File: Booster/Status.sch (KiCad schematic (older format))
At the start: 31 parts, among them J601 StatusLED, P601 ~OVERCURRENT_OUT, P602 ~OVERCURRENT_OUT_OP, P603 MSTR_SW, P604 MSTR_SW_OUT, P605 MSTR_SW_OUT_OP, P606 DRIVER_ENABLE_OUT_OP, P607 DRIVER_ENABLE_OUT, Q601 BC327, Q602 BC327, Q603 BC327, SW601 MSTR_SW, U601 74HC00, U602 PC817, U603 PC817, U604 PC817

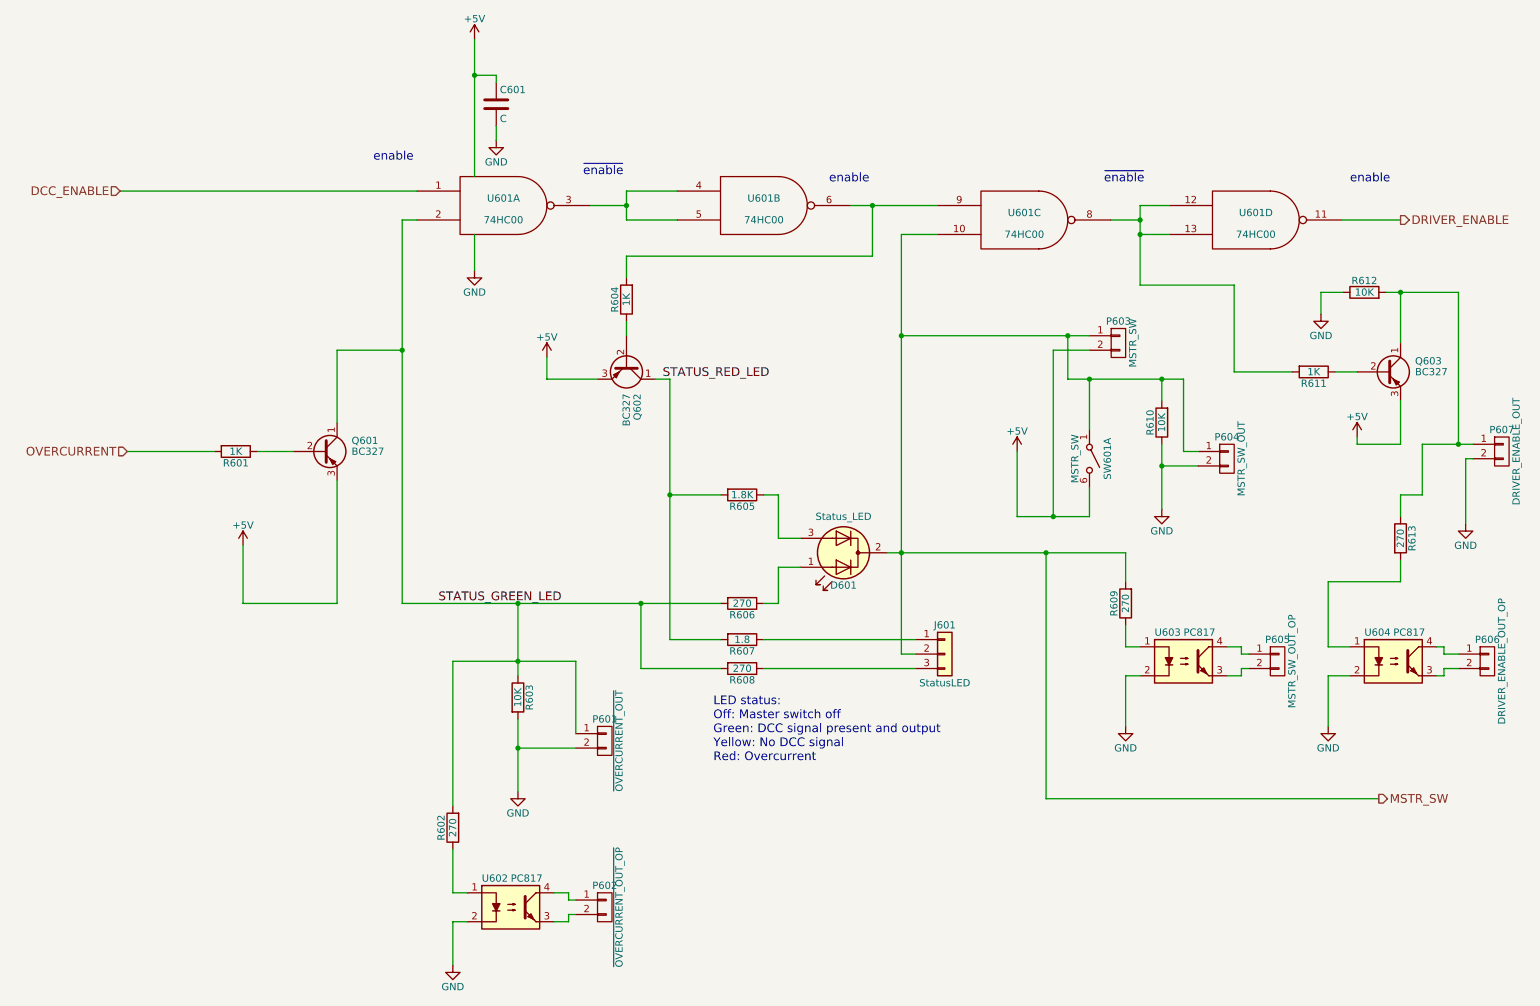
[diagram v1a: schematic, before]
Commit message: Various adjustments based on breadboard prototype.
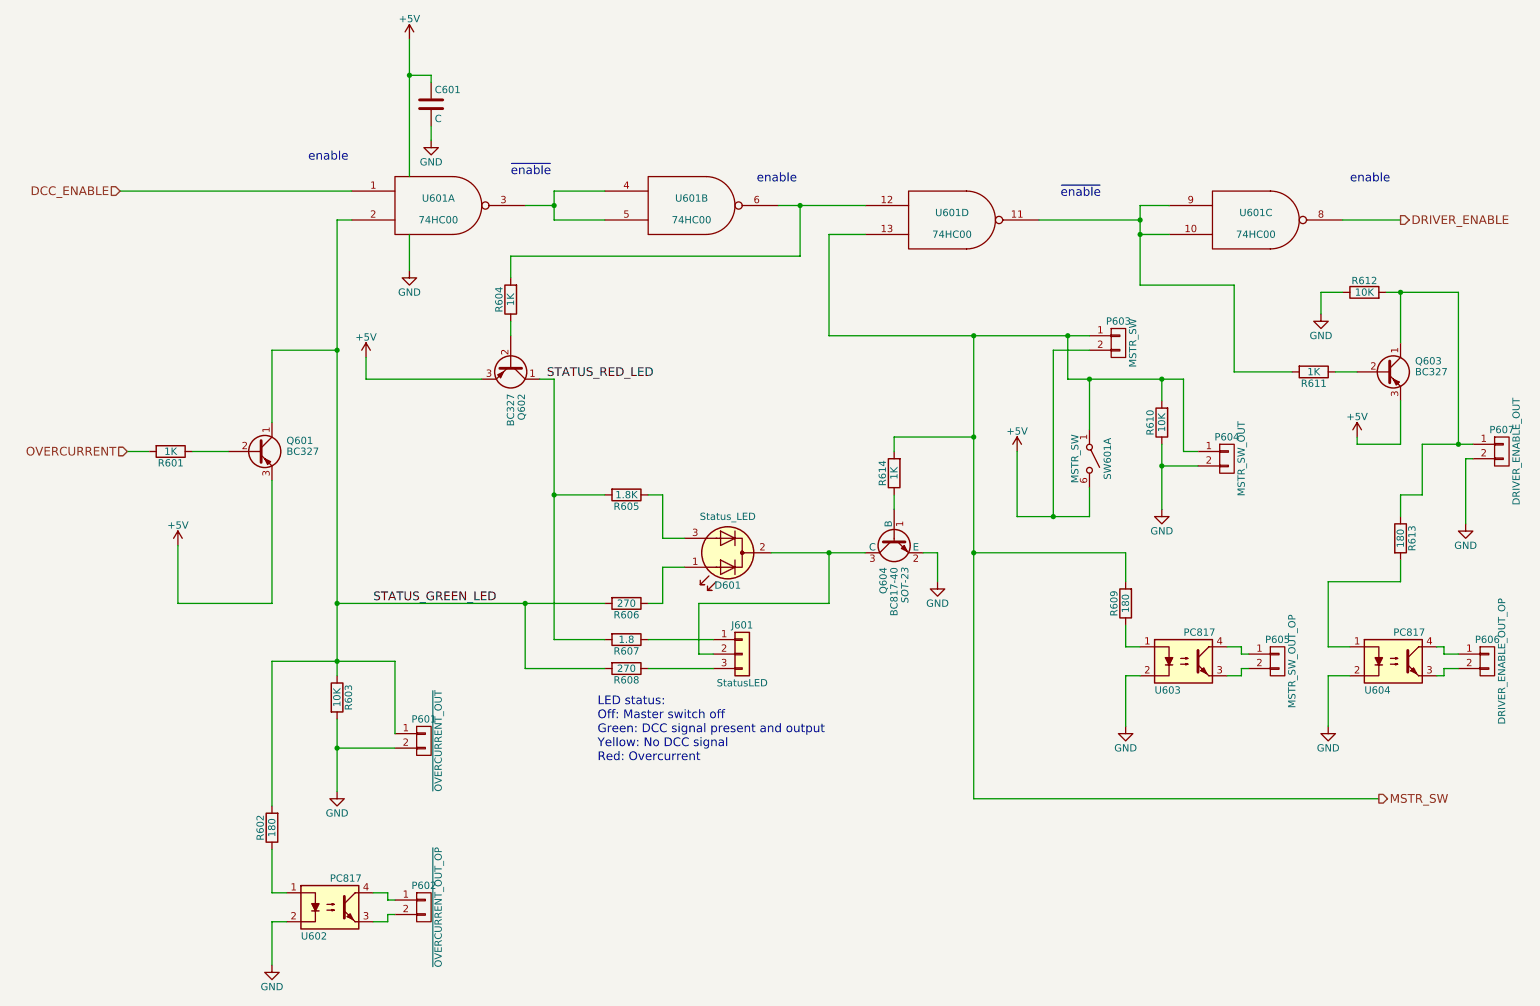
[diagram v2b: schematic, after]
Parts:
- added Q604: BC817-40, SOT-23, symbol BC817-40
- added R614: 1K, symbol R
- R602, R609, R613: value 270 -> 180
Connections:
- net DRIVER_ENABLE: now also U601.8; no longer U601.11
- net GND: now also Q604.2 (E)
- net MSTR_SW: now also U601.13, R614.2; no longer D601.2 (K), J601.2 (Pin_2), U601.10
- net at R604.2, U601.6: now also U601.12; no longer U601.9
- new net: D601.2 (K), J601.2 (Pin_2), Q604.3 (C)
- new net: R611.2, U601.10, U601.11, U601.9
- new net: Q604.1 (B), R614.1
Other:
- moved on the sheet: C601, D601, J601, P601, P602, Q601, Q602, R601, R602, R603, R604, R605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

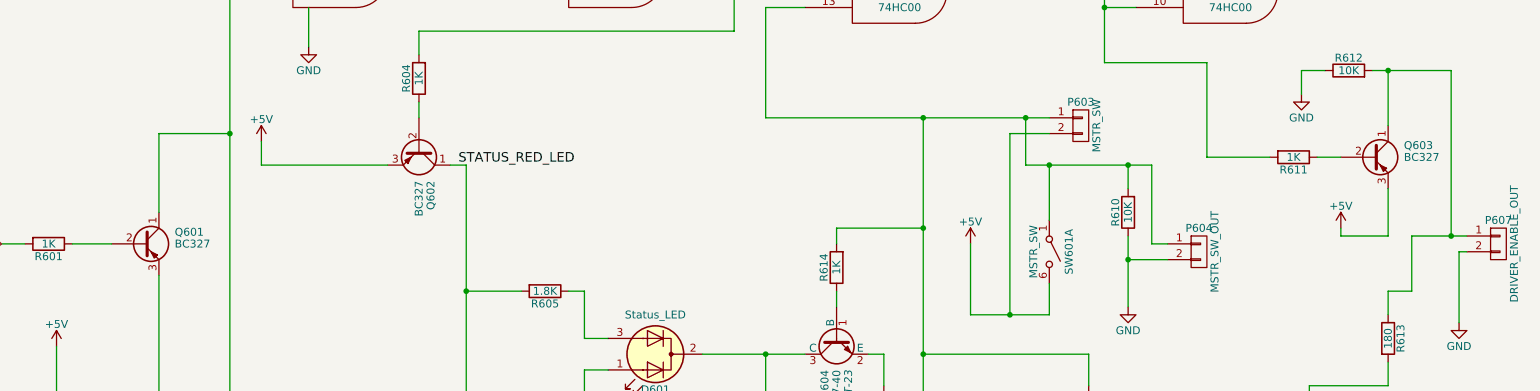
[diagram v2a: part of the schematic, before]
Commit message: Changed to SMD components. Train is now moving. :)
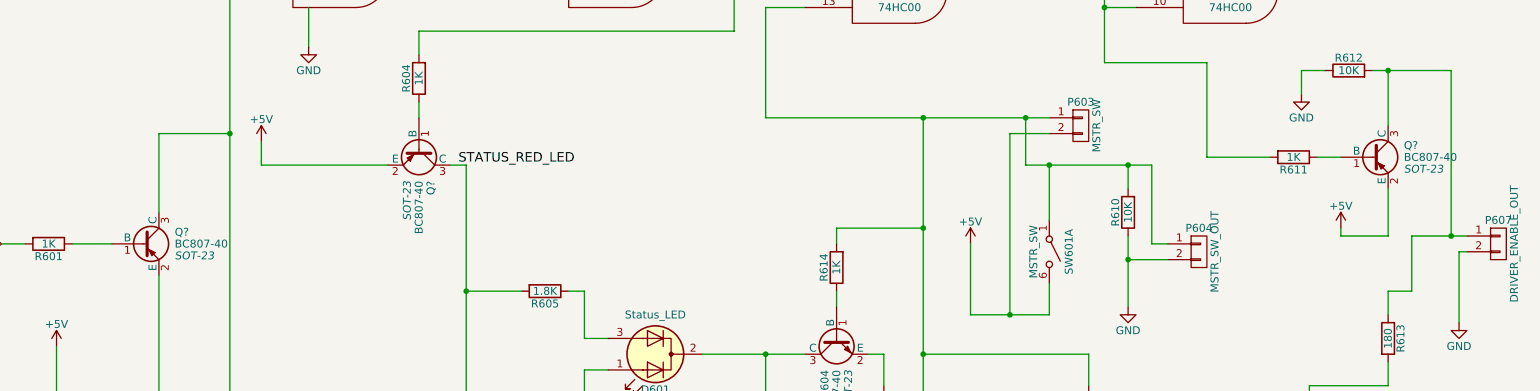
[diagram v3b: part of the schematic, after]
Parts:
- removed Q601, Q602, Q603: BC327, TO_SOT_Packages_THT:TO-92_Molded_Narrow, symbol BC327
- added Q? (x3): BC807-40, SOT-23, symbol BC807-40
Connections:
- net +5V: now also Q?.2 (E), Q?.2 (E), Q?.2 (E)
- net STATUS_GREEN_LED: now also Q?.3 (C)
- net STATUS_RED_LED: now also Q?.3 (C)
- net at R601.1: now also Q?.1 (B)
- net at R604.1: now also Q?.1 (B)
- net at R611.1: now also Q?.1 (B)
- net at P607.1 (P1), R612.2, R613.1: now also Q?.3 (C)
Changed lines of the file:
@@
-$EndComp
-$Comp
-L BC327 Q601
-U 1 1 5A0BE3D7
-P 2350 3650
-F 0 "Q601" H 2550 3725 50  0000 L CNN
-F 1 "BC327" H 2550 3650 50  0000 L CNN
-F 2 "TO_SOT_Packages_THT:TO-92_Molded_Narrow" H 2550 3575 50  0001 L CIN
-F 3 "" H 2350 3650 50  0001 L CNN
-	1    2350 3650
-	1    0    0    -1
 $EndComp
 $Comp
@@
 $EndComp
 $Comp
-L BC327 Q602
-U 1 1 5A0BE943
-P 4100 3050
-F 0 "Q602" H 4300 3125 50  0000 L CNN
-F 1 "BC327" H 4300 3050 50  0000 L CNN
-F 2 "TO_SOT_Packages_THT:TO-92_Molded_Narrow" H 4300 2975 50  0001 L CIN
-F 3 "" H 4100 3050 50  0001 L CNN
-	1    4100 3050
-	0    1    1    0
-$EndComp
-$Comp
 L R R605
 U 1 1 5A0BEB8F
@@
 $EndComp
 $Comp
-L BC327 Q603
-U 1 1 5A0DFF91
-P 10150 3100
-F 0 "Q603" H 10350 3175 50  0000 L CNN
-F 1 "BC327" H 10350 3100 50  0000 L CNN
-F 2 "TO_SOT_Packages_THT:TO-92_Molded_Narrow" H 10350 3025 50  0001 L CIN
-F 3 "" H 10150 3100 50  0001 L CNN
-	1    10150 3100
-	1    0    0    -1
-$EndComp
-$Comp
 L CONN_01X02 P607
 U 1 1 5A0E0030
@@
 Wire Wire Line
 	7050 4350 7050 4550
+$Comp
+L BC807-40 Q?
+U 1 1 5A3E8EA3
+P 10150 3100
+F 0 "Q?" H 10350 3175 50  0000 L CNN
+F 1 "BC807-40" H 10350 3100 50  0000 L CNN
+F 2 "SOT-23" H 10350 3025 50  0000 L CIN
+F 3 "" H 10150 3100 50  0000 L CNN
+	1    10150 3100
+	1    0    0    -1
+$EndComp
+$Comp
+L BC807-40 Q?
+U 1 1 5A3E9138
+P 4100 3050
+F 0 "Q?" H 4300 3125 50  0000 L CNN
+F 1 "BC807-40" H 4300 3050 50  0000 L CNN
+F 2 "SOT-23" H 4300 2975 50  0000 L CIN
+F 3 "" H 4100 3050 50  0000 L CNN
+	1    4100 3050
+	0    1    1    0
+$EndComp
+$Comp
+L BC807-40 Q?
+U 1 1 5A3E9B01
+P 2350 3650
+F 0 "Q?" H 2550 3725 50  0000 L CNN
+F 1 "BC807-40" H 2550 3650 50  0000 L CNN
+F 2 "SOT-23" H 2550 3575 50  0000 L CIN
+F 3 "" H 2350 3650 50  0000 L CNN
+	1    2350 3650
+	1    0    0    -1
+$EndComp
 $EndSCHEMATC
